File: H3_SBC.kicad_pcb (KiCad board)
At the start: 6 copper layers, 50 x 40 mm, 181 parts, among them CN1 YXT-BB10-50P-02, CN2 YXT-BB10-50P-02, CN3 YXT-BB10-50P-02, Q1 WPM1481-6/TR, U1 H3, U10 XT28EG32GA4YJECGA, U2 AXP223_C2997893, U3 K4B4G1646E-BYMA 4GB, U4 K4B4G1646E-BYMA 4GB, U5 AP2127K-2.5, U9 RTL8211E-VB-CG, X1 X201232768KLD2SI, X2 SMD-5032_4P 24M 20pf, X3 5YAA25000121TF25E2

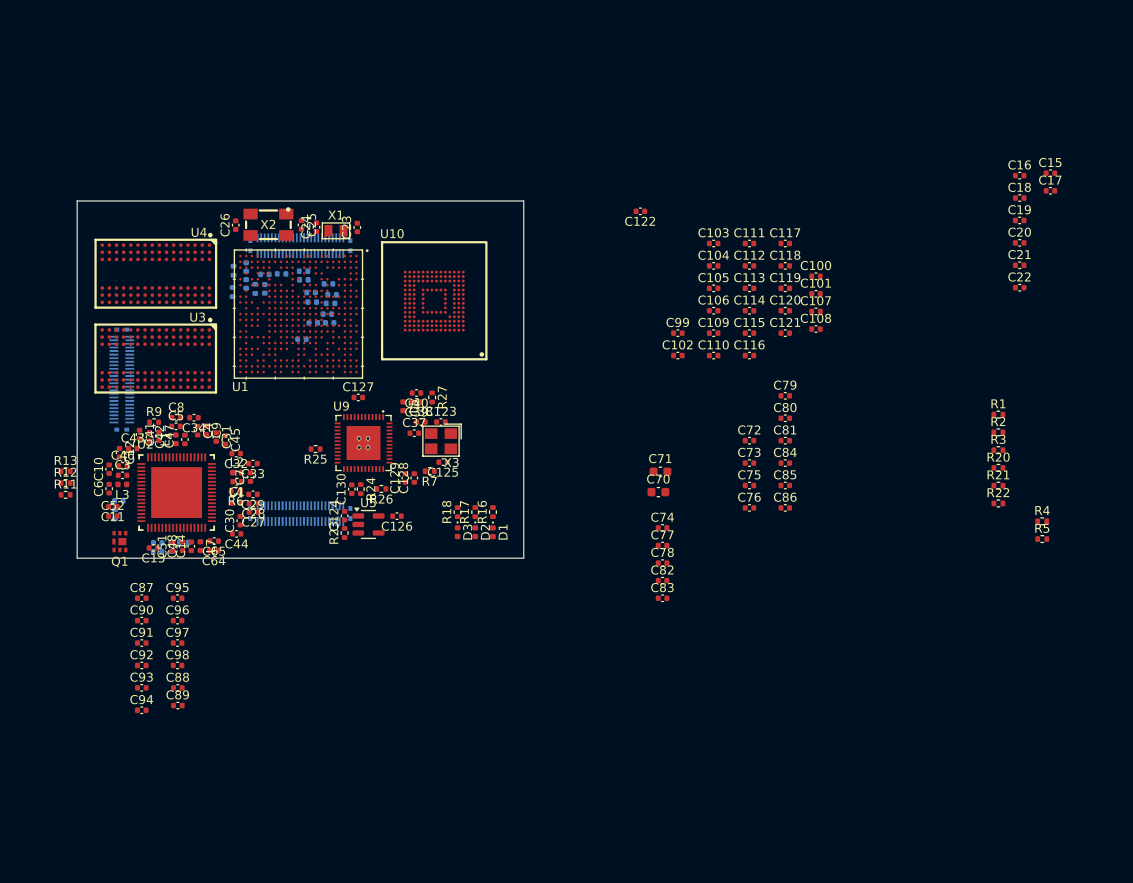
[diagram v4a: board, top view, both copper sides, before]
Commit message: started RAM routing, might move to 1 module though
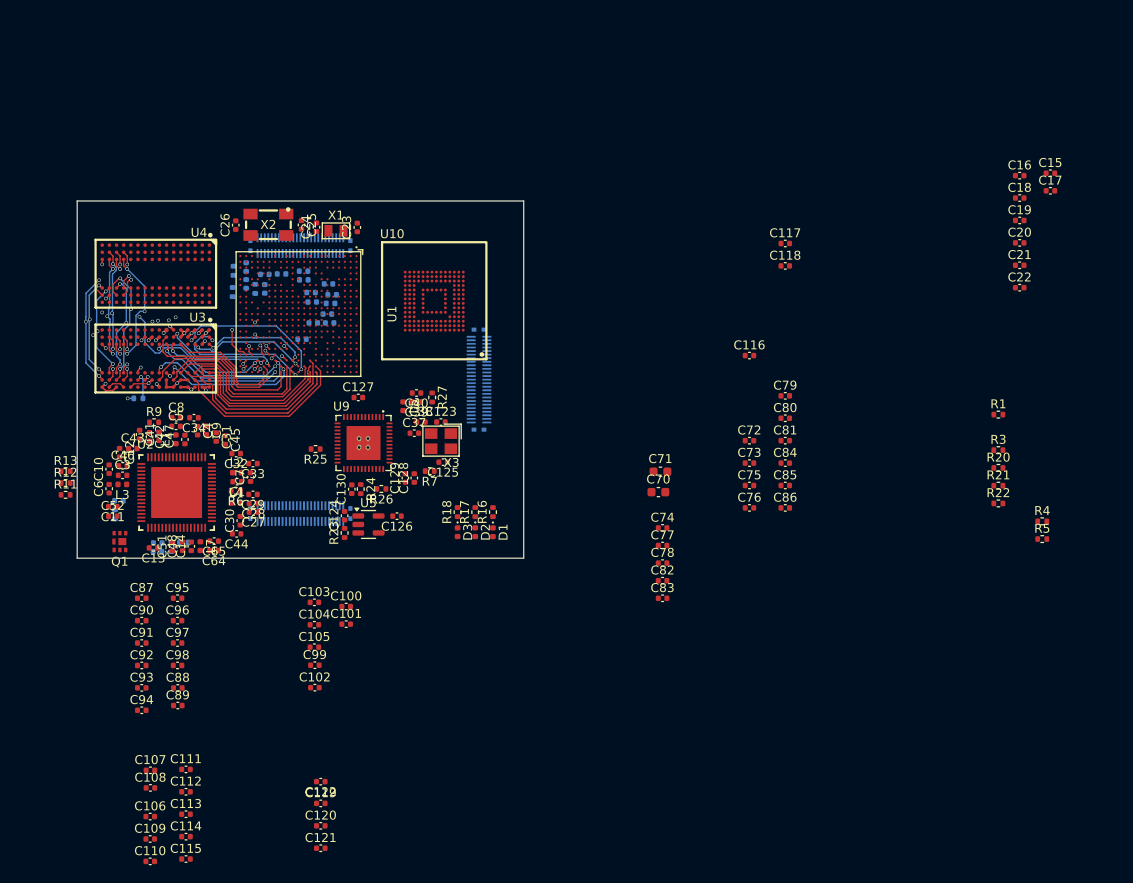
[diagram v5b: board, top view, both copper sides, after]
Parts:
- R2: moved to B.Cu
- U1: footprint H3:BGA347_H3_AWT -> easyeda2kicad:BGA-347_L14.0-W14.0-R21-C21-P0.65-TL
- moved R2 96.4 mm to (106.8, 72.1), turned to 180 degrees
- moved C107 90.5 mm to (108.2, 113.8)
- moved C108 90.5 mm to (108.2, 115.7)
- moved C111 86.3 mm to (112.2, 113.6)
- moved C112 86.3 mm to (112.2, 116.2)
- moved C113 86.3 mm to (112.2, 118.7)
- moved C114 86.3 mm to (112.2, 121.2)
- moved C115 86.3 mm to (112.2, 123.7)
- moved C106 84.8 mm to (108.2, 118.9)
- moved C109 84.8 mm to (108.2, 121.4)
- moved C110 84.8 mm to (108.2, 124.0)
- moved C119 77.7 mm to (127.3, 117.5)
- moved C120 77.7 mm to (127.3, 120.0)
- moved C121 77.7 mm to (127.3, 122.5)
- moved C122 73.2 mm to (127.3, 115.0)
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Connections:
- net /RAM/SDQS0_N renamed /RAM/SDQS0-
- net /RAM/SDQS0_P renamed /RAM/SDQS0+
- net /RAM/SDQS1_P renamed /RAM/SDQS1+
- net /RAM/SDQS2_P renamed /RAM/SDQS2+
- net /RAM/SDQS3_N renamed /RAM/SDQS3-
- net /RAM/SDQS3_P renamed /RAM/SDQS3+
- U1 pad A13: unconnected-(U1A-PA20-PadA13) -> PA20
- U1 pad A14: unconnected-(U1A-PA21-PadA14) -> PA21
- U1 pad A2: EPHY_LINK_LED -> unconnected-(U1A-EPHY_LINK_LE-PadA2)
- U1 pad AA5: unconnected-(U1A-KEYADC-PadAA5) -> Net-(U1A-KEYADC)
- U1 pad AA6: unconnected-(U1A-NMI-PadAA6) -> Net-(U1A-NMI)
- U1 pad B1: unconnected-(U1B-PG13-PadB1) -> PG11
- U1 pad B13: unconnected-(U1A-PA18-PadB13) -> PA18
- U1 pad B14: unconnected-(U1A-PA19-PadB14) -> PA19
- U1 pad B15: unconnected-(U1H-PC3/NAND_CE1-PadB15) -> SPI0_CS
- U1 pad B16: unconnected-(U1H-PC2/NAND_CLE-PadB16) -> SPI0_CLK
- U1 pad C1: unconnected-(U1B-PG5-PadC1) -> PG5
- U1 pad C13: unconnected-(U1A-PA12-PadC13) -> TWI0_SDA
- U1 pad C14: unconnected-(U1A-PA17-PadC14) -> PA17
- U1 pad C15: unconnected-(U1H-PC0/NAND_WE-PadC15) -> SPI0_MOSI
- U1 pad C16: unconnected-(U1H-PC1/NAND_ALE-PadC16) -> SPI0_MISO
- U1 pad C2: unconnected-(U1B-PG4-PadC2) -> PG4
- U1 pad C3: unconnected-(U1B-PG8-PadC3) -> PG8
- U1 pad D11: unconnected-(U1A-PA0-PadD11) -> JTAG_MS
- U1 pad D13: unconnected-(U1A-PA9-PadD13) -> PA9
- U1 pad D15: unconnected-(U1A-PA16-PadD15) -> UART3_CTS
- U1 pad D2: unconnected-(U1B-PG11-PadD2) -> PG11
- U1 pad D3: unconnected-(U1B-PG7-PadD3) -> PG7
- U1 pad D5: unconnected-(U1A-PA1-PadD5) -> JTAG_CK
- U1 pad D6: unconnected-(U1A-PA2-PadD6) -> JTAG_DO
- U1 pad D8: unconnected-(U1A-PA7-PadD8) -> PA7
- U1 pad E11: unconnected-(U1A-PA10-PadE11) -> PA10
- U1 pad E13: unconnected-(U1A-PA3-PadE13) -> JTAG_DI
- U1 pad E14: unconnected-(U1A-PA6-PadE14) -> PA6
- U1 pad E15: unconnected-(U1A-PA13-PadE15) -> UART3_TX
- U1 pad E3: unconnected-(U1B-PG9-PadE3) -> PG9
- U1 pad F10: unconnected-(U1A-TVOUT-PadF10) -> TVOUT
- U1 pad F11: unconnected-(U1A-PA11-PadF11) -> TWI0_SCK
- U1 pad F13: unconnected-(U1A-PA8-PadF13) -> PA8
- U1 pad F14: unconnected-(U1A-PA15-PadF14) -> UART3_RTS
- U1 pad F3: unconnected-(U1B-PG3-PadF3) -> PG3
- U1 pad F5: unconnected-(U1A-PA4-PadF5) -> PA4
- U1 pad F7: EPHY_SPD_LED -> unconnected-(U1A-EPHY_SPD_LE-PadF7)
- U1 pad F8: unconnected-(U1D-EPHY_VDD-PadF8) -> VCC1V2_SYS
- U1 pad G10: unconnected-(U1E-VDD_EFUSE-PadG10) -> VCC3V3
- U1 pad G11: unconnected-(U1D-VCC_USB-PadG11) -> VCC3V3
- U1 pad G12: unconnected-(U1A-PA14-PadG12) -> UART3_RX
- U1 pad G4: unconnected-(U1B-PG6-PadG4) -> PG6
- U1 pad G7: unconnected-(U1D-EPHY_VCC-PadG7) -> VCC3V3
- U1 pad G9: unconnected-(U1D-V33_TV-PadG9) -> VCC3V3_AUDIO
- U1 pad H11: unconnected-(U1E-VDD_EF_USEBP-PadH11) -> Net-(U1E-VDD_EF_USEBP)
- U1 pad H4: unconnected-(U1B-PG2-PadH4) -> PG2
- U1 pad H6: unconnected-(U1A-PA5-PadH6) -> PA5
- U1 pad H7: unconnected-(U1D-VCC_PG-PadH7) -> VCC3V3
- U1 pad J15: unconnected-(U1D-VCC_PD-PadJ15) -> VCC3V3
- U1 pad J20: /RAM/SDQS1_N -> /RAM/SDQS1-
- U1 pad J3: unconnected-(U1B-PG0-PadJ3) -> PG0
- U1 pad J6: unconnected-(U1D-HVCC-PadJ6) -> VCC3V3
- U1 pad K6: unconnected-(U1D-VCC_RTC-PadK6) -> VCC_RTC
- U1 pad L19: MDIO -> RGMII_MDIO
- U1 pad L2: unconnected-(U1B-PG1-PadL2) -> PG1
- U1 pad M1: unconnected-(U1B-PL1-PadM1) -> AXP_SDA
- U1 pad M3: unconnected-(U1B-PG10-PadM3) -> PG10
- U1 pad M4: unconnected-(U1D-RTC_VIO-PadM4) -> VCC1V2_CPU
- U1 pad M5: unconnected-(U1F-HGND-PadM5) -> GND
- U1 pad M6: unconnected-(U1B-PL9-PadM6) -> STATLED_DISK
- U1 pad N1: unconnected-(U1B-PL0-PadN1) -> AXP_IRQ
- U1 pad N3: unconnected-(U1D-VCC_PLL-PadN3) -> VCC3V3
- U1 pad P2: unconnected-(U1B-PL2-PadP2) -> AXP_SCL
- U1 pad T10: unconnected-(U1F-GND-CPUFB-PadT10) -> CPUX_FB
- U1 pad T9: unconnected-(U1F-GND-CPUFB-PadT9) -> GND
- U1 pad U3: unconnected-(U1E-AGND-PadU3) -> GND
- U1 pad V2: unconnected-(U1B-PL10-PadV2) -> STATLED_ERR
- U1 pad V3: unconnected-(U1D-AVCC-PadV3) -> VCC3V3_AUDIO
- U1 pad V4: unconnected-(U1B-VRP-PadV4) -> Net-(U1B-VRP)
- U1 pad V6: unconnected-(U1A-RESET-PadV6) -> AXP_PWROK
- U1 pad W5: unconnected-(U1B-VRA2-PadW5) -> Net-(U1B-VRA2)
- U1 pad W6: unconnected-(U1A-UBOOT-PadW6) -> UBOOT
- U1 pad Y15: /RAM/SDQS1_N -> /RAM/SDQS2-
- U1 pad Y4: unconnected-(U1B-VRA1-PadY4) -> Net-(U1B-VRA1)
- U3 pad B7: /RAM/SDQS1_N -> /RAM/SDQS1-
- U4 pad G3: /RAM/SDQS1_N -> /RAM/SDQS2-
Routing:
- net DDR_A4: track 0.00 -> 41.0 mm, vias 0 -> 4
- net DDR_A14: track 0.00 -> 36.8 mm, vias 0 -> 4
- net DDR_A8: track 0.00 -> 36.4 mm, vias 0 -> 4
- net DDR_A11: track 0.00 -> 36.0 mm, vias 0 -> 4
- net DDR_A2: track 0.00 -> 33.6 mm, vias 0 -> 4
- net DDR_A9: track 0.00 -> 32.9 mm, vias 0 -> 4
- net DDR_A7: track 0.00 -> 31.6 mm, vias 0 -> 4
- net DDR_A12: track 0.00 -> 31.3 mm, vias 0 -> 4
- net DDR_A6: track 0.00 -> 31.3 mm, vias 0 -> 4
- net /RAM/SBA1: track 0.00 -> 31.2 mm, vias 0 -> 4
- net DDR_A13: track 0.00 -> 31.1 mm, vias 0 -> 4
- net DDR_A5: track 0.00 -> 30.7 mm, vias 0 -> 4
- net DDR_A1: track 0.00 -> 30.0 mm, vias 0 -> 4
- net DDR_A3: track 0.00 -> 29.9 mm, vias 0 -> 4
- net DDR_A0: track 0.00 -> 29.9 mm, vias 0 -> 4
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- added copper zone on In1.Cu, net GND

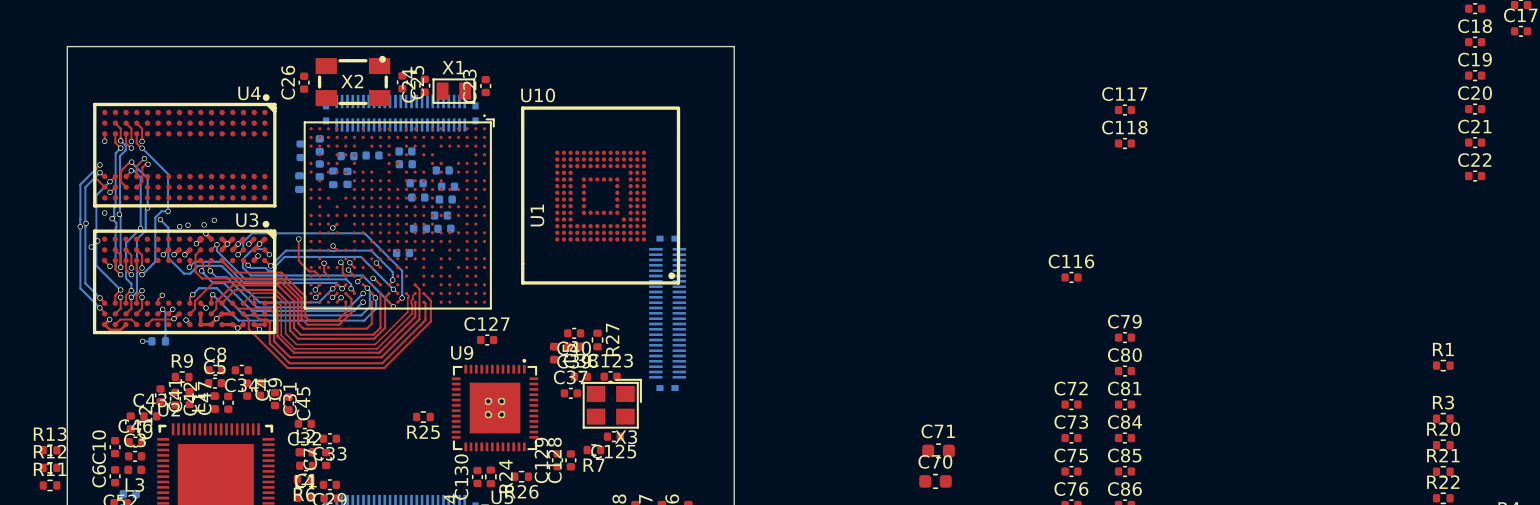
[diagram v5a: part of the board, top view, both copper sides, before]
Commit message: switched to one RAM module
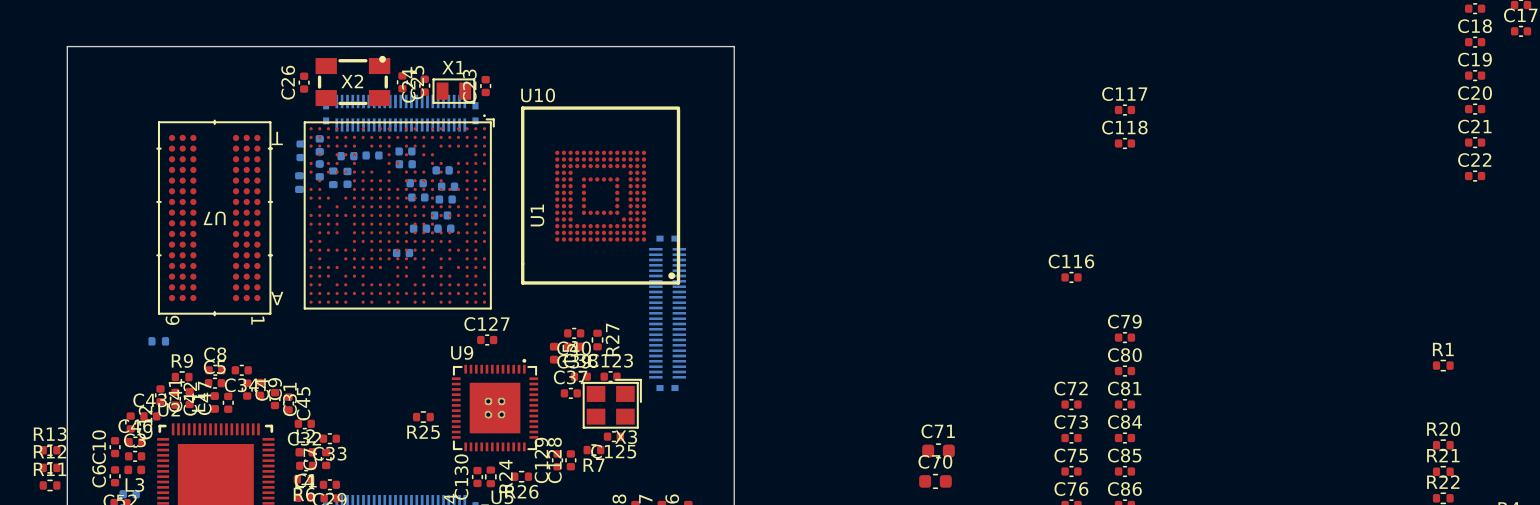
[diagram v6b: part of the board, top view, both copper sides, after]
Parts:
- removed R3: 240R, Resistor_SMD:R_0402_1005Metric
- removed U3, U4: K4B4G1646E-BYMA 4GB, easyeda2kicad:FBGA-96_L13.5-W7.5-R16-C6-P0.80-TL
- added U7: MT41K512M16VRP-107 IT:P, footprints:FBGA96_MRN, F.Cu at (111.0, 62.9)
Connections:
- U1 pad R17: unconnected-(U1C-SA15-PadR17) -> DDR_A15
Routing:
- net DDR_A4: track 41.0 -> 0.00 mm, vias 4 -> 0
- net DDR_A14: track 36.8 -> 0.00 mm, vias 4 -> 0
- net DDR_A8: track 36.4 -> 0.00 mm, vias 4 -> 0
- net DDR_A11: track 36.0 -> 0.00 mm, vias 4 -> 0
- net DDR_A2: track 33.6 -> 0.00 mm, vias 4 -> 0
- net DDR_A9: track 32.9 -> 0.00 mm, vias 4 -> 0
- net DDR_A7: track 31.6 -> 0.00 mm, vias 4 -> 0
- net DDR_A12: track 31.3 -> 0.00 mm, vias 4 -> 0
- net DDR_A6: track 31.3 -> 0.00 mm, vias 4 -> 0
- net /RAM/SBA1: track 31.2 -> 0.00 mm, vias 4 -> 0
- net DDR_A13: track 31.1 -> 0.00 mm, vias 4 -> 0
- net DDR_A5: track 30.7 -> 0.00 mm, vias 4 -> 0
- net DDR_A1: track 30.0 -> 0.00 mm, vias 4 -> 0
- net DDR_A3: track 29.9 -> 0.00 mm, vias 4 -> 0
- net DDR_A0: track 29.9 -> 0.00 mm, vias 4 -> 0
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
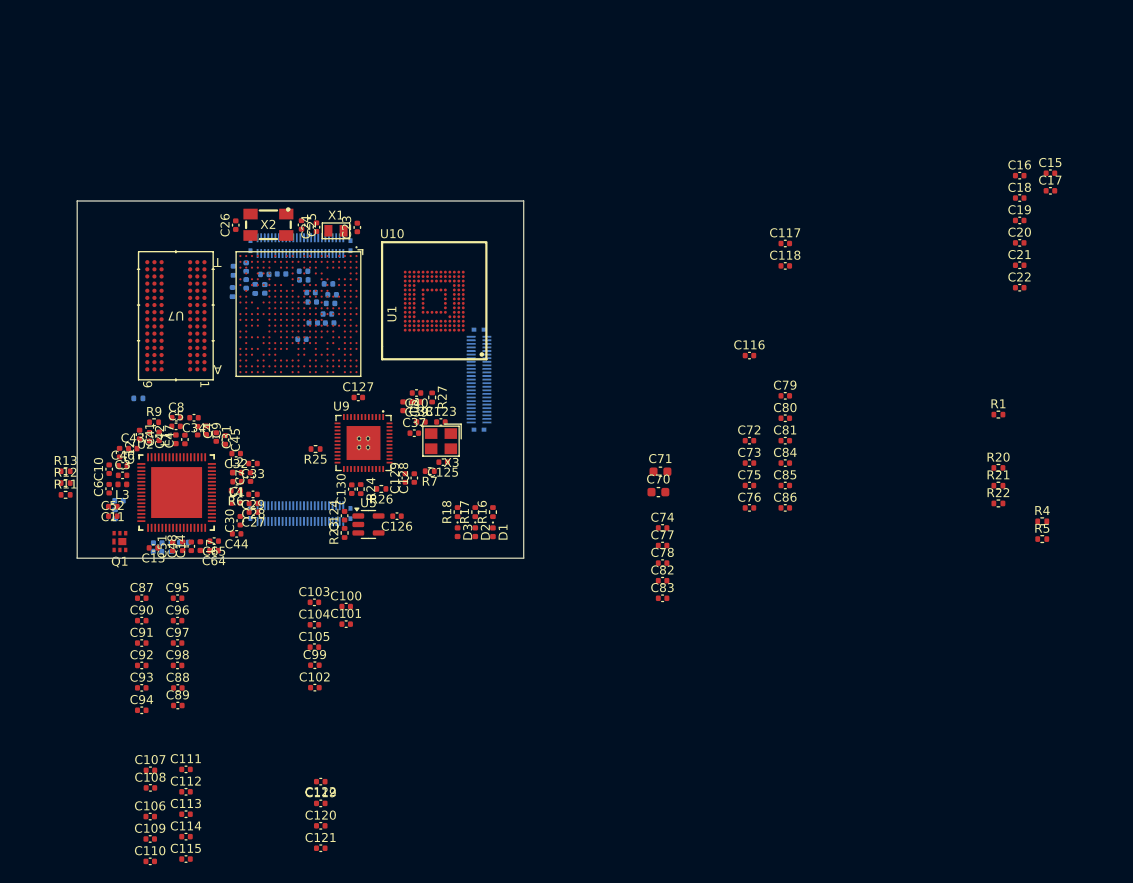
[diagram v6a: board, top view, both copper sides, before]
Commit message: RAM routing additions
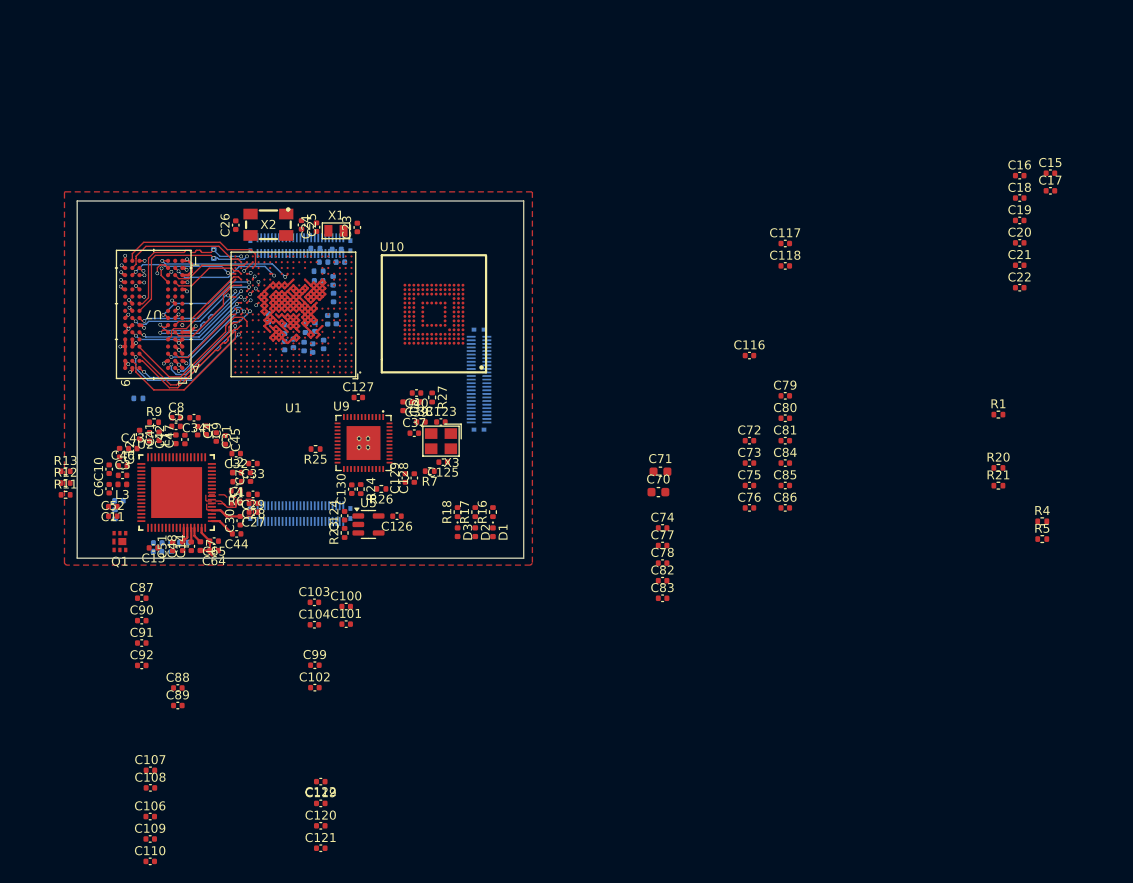
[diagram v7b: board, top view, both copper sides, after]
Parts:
- removed C105, C111, C112, C113, C114, C115, C93, C94, C95, C96, C97, C98: 0.1uF, Capacitor_SMD:C_0402_1005Metric
- R22: moved to B.Cu
- moved R22 92.2 mm to (115.3, 55.9), turned to 90 degrees
- moved R15 11.8 mm to (129.1, 55.4), turned to 0 degrees
- moved C66 10.6 mm to (129.5, 56.8), turned to 0 degrees
- moved R14 10.5 mm to (126.7, 55.3), turned to 180 degrees
- moved C68 9.00 mm to (127.6, 56.8), turned to 180 degrees
- moved C67 7.69 mm to (128.7, 58.9), turned to -90 degrees
- moved R19 7.36 mm to (127.0, 57.9), turned to 180 degrees
- moved C60 6.80 mm to (127.6, 66.1), turned to 90 degrees
- moved C58 6.54 mm to (129.0, 63.3), turned to -90 degrees
- moved C61 6.40 mm to (128.7, 60.8), turned to -90 degrees
- moved C56 6.35 mm to (126.4, 66.5), turned to 90 degrees
- moved C69 6.10 mm to (127.0, 58.9), turned to 180 degrees
- moved C63 5.67 mm to (125.4, 66.3), turned to 90 degrees
- moved C36 5.65 mm to (123.2, 66.2), turned to 90 degrees
- moved C57 5.21 mm to (128.0, 63.3), turned to -90 degrees
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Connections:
- net /RAM/SCK_N renamed /RAM/SCK-
- net /RAM/SCK_P renamed /RAM/SCK+
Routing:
- net GND: track 0.00 -> 81.3 mm, vias 0 -> 14
- net VCC1V5_DRAM: track 0.00 -> 27.6 mm, vias 0 -> 14
- net DDR_A14: track 0.00 -> 20.4 mm, vias 0 -> 2
- net DDR_A11: track 0.00 -> 19.9 mm, vias 0 -> 2
- net VCC1V2_CPU: track 0.00 -> 18.5 mm
- net /RAM/SCK+: track 0.00 -> 17.5 mm, vias 0 -> 2
- net SDQ8: track 0.00 -> 17.3 mm
- net DDR_A8: track 0.00 -> 17.3 mm
- net /RAM/SCK-: track 0.00 -> 17.3 mm, vias 0 -> 2
- net SDQ10: track 0.00 -> 16.5 mm
- net SDQ9: track 0.00 -> 16.4 mm, vias 0 -> 2
- net /RAM/SDQS1+: track 0.00 -> 16.2 mm
- net /RAM/SDQS1-: track 0.00 -> 16.2 mm
- net DDR_A13: track 0.00 -> 15.6 mm, vias 0 -> 2
- net DDR_A15: track 0.00 -> 15.6 mm, vias 0 -> 2
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- added copper zone on F.Cu, net GND
- added copper zone on F.Cu, net Net-(L4-Pad1)
- added copper zone on F.Cu, net VCC1V5_DRAM

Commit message: power routing additions
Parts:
- C53: moved to F.Cu
- moved C53 2.46 mm to (102.2, 84.0), turned to 90 degrees
- moved C34 1.42 mm to (114.5, 74.3), turned to 0 degrees
- moved R10 1.19 mm to (103.2, 85.8)
- moved C50 1.01 mm to (109.0, 88.2)
- moved C49 0.96 mm to (109.0, 89.2)
- moved C52 0.87 mm to (103.2, 85.8), turned to 90 degrees
- moved C3 0.51 mm to (105.1, 81.2)
- moved L3 0.51 mm to (105.1, 82.2)
- moved C4 0.49 mm to (113.0, 75.7)
- moved C9 0.49 mm to (114.0, 75.7)
- moved L6 0.27 mm to (112.2, 88.2)
- moved Q1 0.26 mm to (104.5, 88.1), turned to 0 degrees
- moved C10 0.22 mm to (103.6, 80.2), turned to -90 degrees
- moved R8 0.16 mm to (110.7, 88.7), turned to 90 degrees
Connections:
- CN1 pad 27: PWR_ON -> GND
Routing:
- net GND: track 81.3 -> 103.9 mm, vias 14 -> 15
- net /Power/IPSOUT: track 7.95 -> 24.0 mm, vias 0 -> 2
- net /Power/CHSENCEN: track 0.00 -> 14.8 mm, vias 0 -> 2
- net +BATT: track 0.00 -> 6.41 mm, vias 0 -> 1
- net /Power/CHSENCEP: track 0.00 -> 6.03 mm, vias 0 -> 1
- net DLDO4: track 0.00 -> 5.89 mm, vias 0 -> 1
- net /Power/N_BATDRV: track 0.00 -> 5.12 mm, vias 0 -> 2
- net DLDO3: track 0.00 -> 4.31 mm
- net NTC: track 0.00 -> 4.23 mm
- net VCC3V3: track 14.3 -> 18.2 mm, vias 0 -> 3
- net Net-(L3-Pad1): track 0.00 -> 3.79 mm
- net /Power/LX_CHG: track 0.00 -> 3.75 mm, vias 0 -> 1
- net VCC1V2_SYS: track 12.0 -> 15.6 mm, vias 0 -> 2
- net DLDO1: track 0.00 -> 3.45 mm, vias 0 -> 1
- net Net-(U2A-VINT): track 0.00 -> 2.87 mm
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- added copper zone on F.Cu, net +5V
- added copper zone on F.Cu, net /Power/CHSENCEN
- added copper zone on F.Cu, net /Power/IPSOUT
- added copper zone on F.Cu, net Net-(L1-Pad1)
- added copper zone on F.Cu, net VCC1V2_CPU
- added copper zone on F.Cu, net VCC1V2_SYS
- added copper zone on F.Cu, net VCC3V3
- added copper zone on F.Cu, net VCC3V3_AUDIO
